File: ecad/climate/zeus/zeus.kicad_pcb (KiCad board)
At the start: 2 copper layers, 80 x 45 mm, 76 parts, among them J1 MCV 1,5/ 2-G-3,5, J10 47053-1000, J11 47053-1000, J2 MCV 1,5/ 2-G-3,5, J3 MCV 1,5/ 2-G-3,5, J4 M20-8760342, J5 47053-1000, J6 47053-1000, J7 215079-8, J8 640454-2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

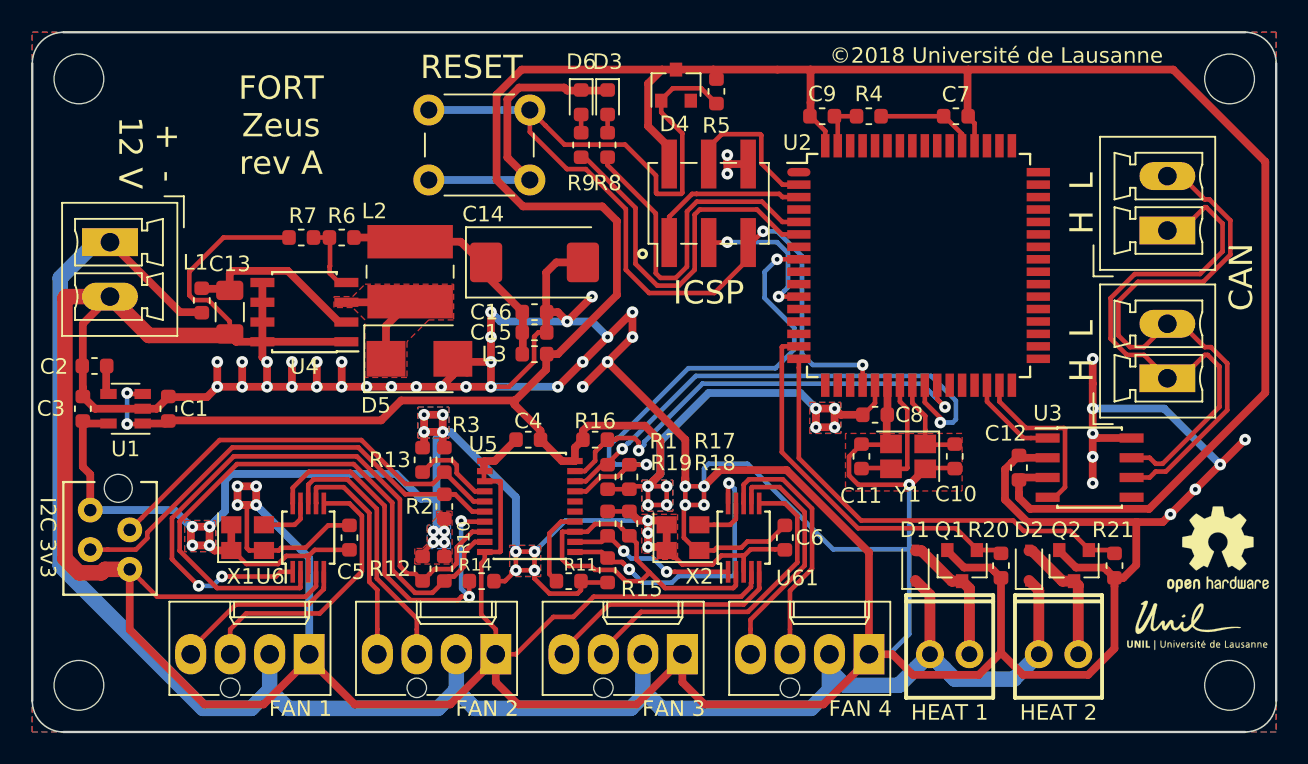
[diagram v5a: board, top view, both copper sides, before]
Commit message: Updates climate board to rev B~dev
 * Changes all Power Connectors to MiniFit-JR 5566-02A to avoid
   someone pluging the power supply on the CAN bus as it will destroy
   all MCP2561 on the bus
 * Fixes issues in Arke:
 ** Crossed Rx/Tx lines
 ** Flipped DB9 connector
 * Fixes and Improvment in Celaeno/Zeus:
 ** Added missing pull-up resistor on tachometer inputs
 ** Removed unecessary 32.268kHz oscillators (they are not working
    properly with manual soldering)
 ** Removed I2C multiplexer as we can add a second EMC2302 with a
   different i2c address to do the same thing. Repaced it by an i2c
   level shifter (tested and working).

Many of these changes still need to be tested before going to
production
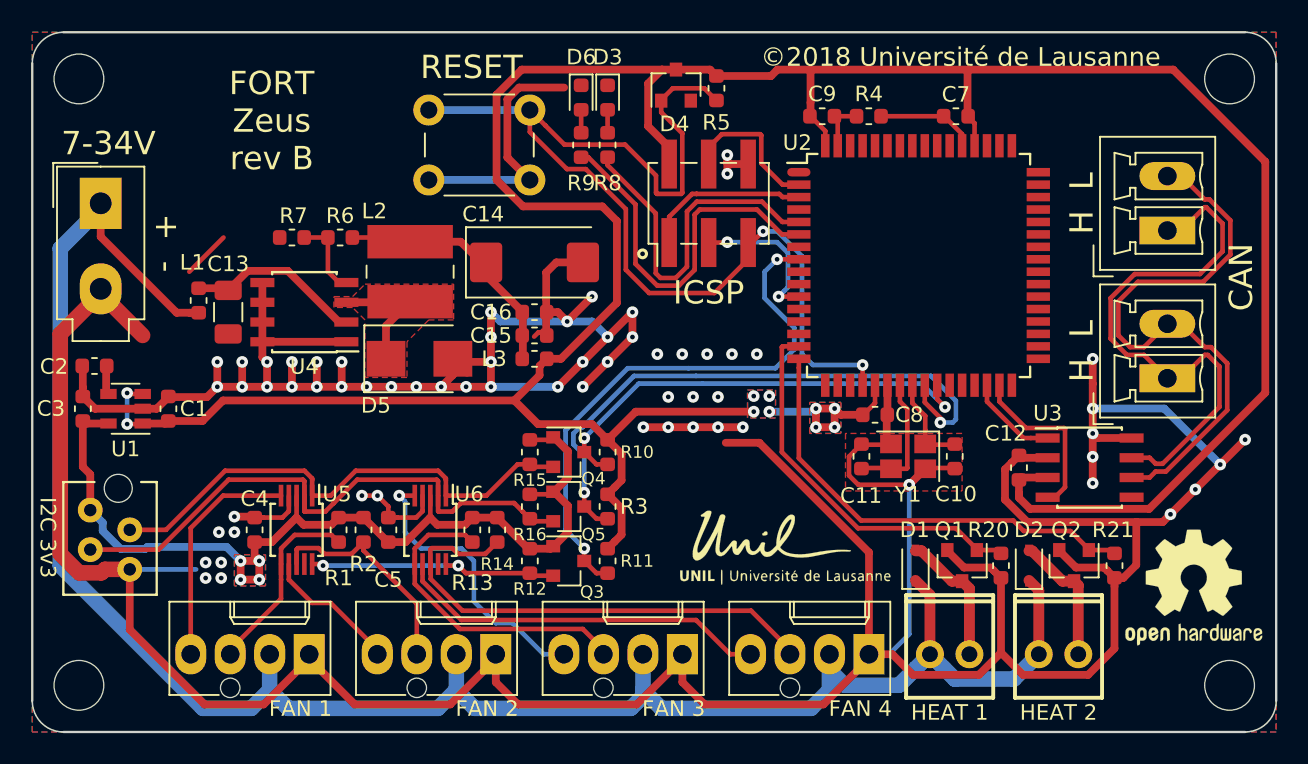
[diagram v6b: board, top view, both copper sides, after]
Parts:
- removed C6: 100nF, Capacitor_SMD:C_0603_1608Metric
- removed the G*** at (175.0, 143.2)
- removed R17, R18, R19: 10k, Resistor_SMD:R_0603_1608Metric
- removed REF***: OSHW-Logo2_7.3x6mm_SilkScreen, Symbols:OSHW-Logo2_7.3x6mm_SilkScreen
- removed U61: EMC2302-1-AIZL-TR, Package_SO:MSOP-10_3x3mm_P0.5mm
- removed X1, X2: 32.768kHz, Oscillator:Oscillator_SMD_Abracon_ASE-4Pin_3.2x2.5mm
- added G***: LOGO, FORT:UNIL-LOGO_13.8x5.1mm, F.Cu at (148.6, 138.3)
- added Q3: BSS138, Package_TO_SOT_SMD:SOT-23, F.Cu at (134.5, 139.0)
- added Q4: BSS138, Package_TO_SOT_SMD:SOT-23, F.Cu at (134.5, 132.0)
- added Q5: BSS138, Package_TO_SOT_SMD:SOT-23, F.Cu at (134.5, 135.5)
- added REF**: OSHW-Logo2_9.8x8mm_SilkScreen, Symbol:OSHW-Logo2_9.8x8mm_SilkScreen, F.Cu at (174.7, 140.7)
- J3: value MCV 1,5/ 2-G-3,5 -> 5566-02A; footprint Connector_Phoenix_MC:PhoenixContact_MCV_1,5_2-G-3.5_1x02_P3.50mm_Vertical -> FORT:Molex_Mini-Fit_Jr_5566-02A_2x01_P4.20mm_Vertical
- R12, R15, R16: value 10k -> 4k99
- R2, R3: value 4k99 -> 10k
- U5: value TCA9544A -> EMC2302-1-AIZL-TR; footprint Package_SO:SSOP-20_4.4x6.5mm_P0.65mm -> Package_SO:MSOP-10_3x3mm_P0.5mm
- U6: value EMC2302-1-AIZL-TR -> EMC2302-2-AIZL-TR
- moved C4 18.5 mm to (114.3, 137.0), turned to 90 degrees
- moved R1 17.6 mm to (119.7, 137.0)
- moved U5 15.1 mm to (117.0, 137.0), turned to 270 degrees
- moved R10 12.9 mm to (137.0, 132.0), turned to 270 degrees
- moved R3 10.9 mm to (137.0, 135.5), turned to 270 degrees
- moved R15 9.10 mm to (132.0, 132.0)
- moved U6 7.87 mm to (125.6, 137.0), turned to 270 degrees
- moved R12 6.92 mm to (132.0, 139.0), turned to 270 degrees
- moved R16 6.01 mm to (132.0, 135.5), turned to 270 degrees
- moved R13 5.52 mm to (128.3, 137.0), turned to 270 degrees
- moved R2 5.41 mm to (121.3, 137.0)
- moved R14 3.45 mm to (129.9, 137.0), turned to 270 degrees
- moved R11 2.82 mm to (137.0, 139.0), turned to 270 degrees
- moved J3 2.57 mm to (104.4, 116.0), turned to 0 degrees
- moved C5 2.55 mm to (122.9, 137.0)
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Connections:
- C4 pad 1: +5V -> +3V3
- J10 pad 3: /Fan PWM Controller 2/TACH1 -> /Fan PWM Controller 1/TACH3
- J10 pad 4: /Fan PWM Controller 2/PWM1 -> /Fan PWM Controller 1/PWM3
- J11 pad 3: /Fan PWM Controller 2/TACH2 -> /Fan PWM Controller 1/TACH4
- J11 pad 4: /Fan PWM Controller 2/PWM2 -> /Fan PWM Controller 1/PWM4
- J7 pad 2: /I2C Multiplexer/SDA_3V3_0 -> /Fan PWM Controller 1/SDA
- J7 pad 3: /I2C Multiplexer/SCL_3V3_0 -> /Fan PWM Controller 1/SCL
- R1 pad 1: /I2C Multiplexer/SCL_5V -> +3V3
- R1 pad 2: +5V -> /Fan PWM Controller 1/TACH1
- R10 pad 1: /Fan PWM Controller 1/SCL -> +5V
- R10 pad 2: +3V3 -> /I2C Level Shifter/SDA_5V
- R11 pad 1: +3V3 -> +5V
- R11 pad 2: /I2C Multiplexer/~INT3 -> /UC/~FAN_ALERT
- R12 pad 1: /Fan PWM Controller 1/SDA -> +3V3
- R12 pad 2: +3V3 -> /Fan PWM Controller 1/~ALERT
- R13 pad 1: /I2C Multiplexer/~INT0 -> +3V3
- R13 pad 2: +3V3 -> /Fan PWM Controller 1/TACH3
- R14 pad 1: /Fan PWM Controller 1/~ALERT -> +3V3
- R14 pad 2: +3V3 -> /Fan PWM Controller 1/TACH4
- R15 pad 1: /Fan PWM Controller 2/~ALERT -> +3V3
- R15 pad 2: +3V3 -> /Fan PWM Controller 1/SDA
- R16 pad 1: /I2C Multiplexer/SDA_5V -> +3V3
- R16 pad 2: +5V -> /Fan PWM Controller 1/SCL
- R2 pad 1: /I2C Multiplexer/SCL_3V3_0 -> +3V3
- R2 pad 2: +3V3 -> /Fan PWM Controller 1/TACH2
- R3 pad 1: /I2C Multiplexer/SDA_3V3_0 -> +5V
- R3 pad 2: +3V3 -> /I2C Level Shifter/SCL_5V
- U2 pad 25: /I2C Multiplexer/SCL_5V -> /I2C Level Shifter/SCL_5V
- U2 pad 26: /I2C Multiplexer/SDA_5V -> /I2C Level Shifter/SDA_5V
- U5 pad 1: GND -> /Fan PWM Controller 1/SDA
- U5 pad 10: GND -> /Fan PWM Controller 1/~ALERT
- U5 pad 2: GND -> /Fan PWM Controller 1/SCL
- U5 pad 3: GND -> +3V3
- U5 pad 4: /I2C Multiplexer/~INT0 -> GND
- U5 pad 5: /I2C Multiplexer/SDA_3V3_0 -> /Fan PWM Controller 1/PWM1
- U5 pad 6: /I2C Multiplexer/SCL_3V3_0 -> /Fan PWM Controller 1/TACH1
- U5 pad 7: /Fan PWM Controller 1/~ALERT -> /Fan PWM Controller 1/PWM2
- U5 pad 8: /Fan PWM Controller 1/SDA -> /Fan PWM Controller 1/TACH2
- U5 pad 9: /Fan PWM Controller 1/SCL -> (no net)
- U6 pad 5: /Fan PWM Controller 1/PWM1 -> /Fan PWM Controller 1/PWM3
- U6 pad 6: /Fan PWM Controller 1/TACH1 -> /Fan PWM Controller 1/TACH3
- U6 pad 7: /Fan PWM Controller 1/PWM2 -> /Fan PWM Controller 1/PWM4
- U6 pad 8: /Fan PWM Controller 1/TACH2 -> /Fan PWM Controller 1/TACH4
- U6 pad 9: /Fan PWM Controller 1/32K768_CLK -> (no net)
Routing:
- net GND: track 501.3 -> 370.7 mm, vias 50 -> 64
- net +3V3: track 119.3 -> 62.7 mm, vias 19 -> 4
- net /I2C Level Shifter/SCL_5V: track 0.00 -> 38.7 mm, vias 0 -> 2
- net /I2C Multiplexer/SCL_5V: track 33.1 -> 0.00 mm, vias 2 -> 0
- net /Fan PWM Controller 1/TACH4: track 0.00 -> 32.0 mm
- net /I2C Multiplexer/SCL_3V3_0: track 30.0 -> 0.00 mm
- net /I2C Multiplexer/SDA_5V: track 29.8 -> 0.00 mm, vias 2 -> 0
- net /I2C Level Shifter/SDA_5V: track 0.00 -> 29.6 mm, vias 0 -> 2
- net /I2C Multiplexer/SDA_3V3_0: track 27.7 -> 0.00 mm
- net /Fan PWM Controller 1/PWM4: track 0.00 -> 24.1 mm
- net /Fan PWM Controller 2/SCL: track 22.8 -> 0.00 mm
- net /Fan PWM Controller 2/TACH1: track 20.9 -> 0.00 mm
- net /Fan PWM Controller 1/TACH3: track 0.00 -> 20.7 mm
- net /Fan PWM Controller 1/PWM3: track 0.00 -> 18.9 mm, vias 0 -> 1
- net /Fan PWM Controller 2/~ALERT: track 18.7 -> 0.00 mm, vias 2 -> 0
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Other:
- board text added: "+ -"
- board text added: "7-34V"
- board text added: "FORT Zeus rev B"
- board text removed: "+ - 12 V"
- board text removed: "FORT Zeus rev A"

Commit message: Adds TVS diode on zeus output fan
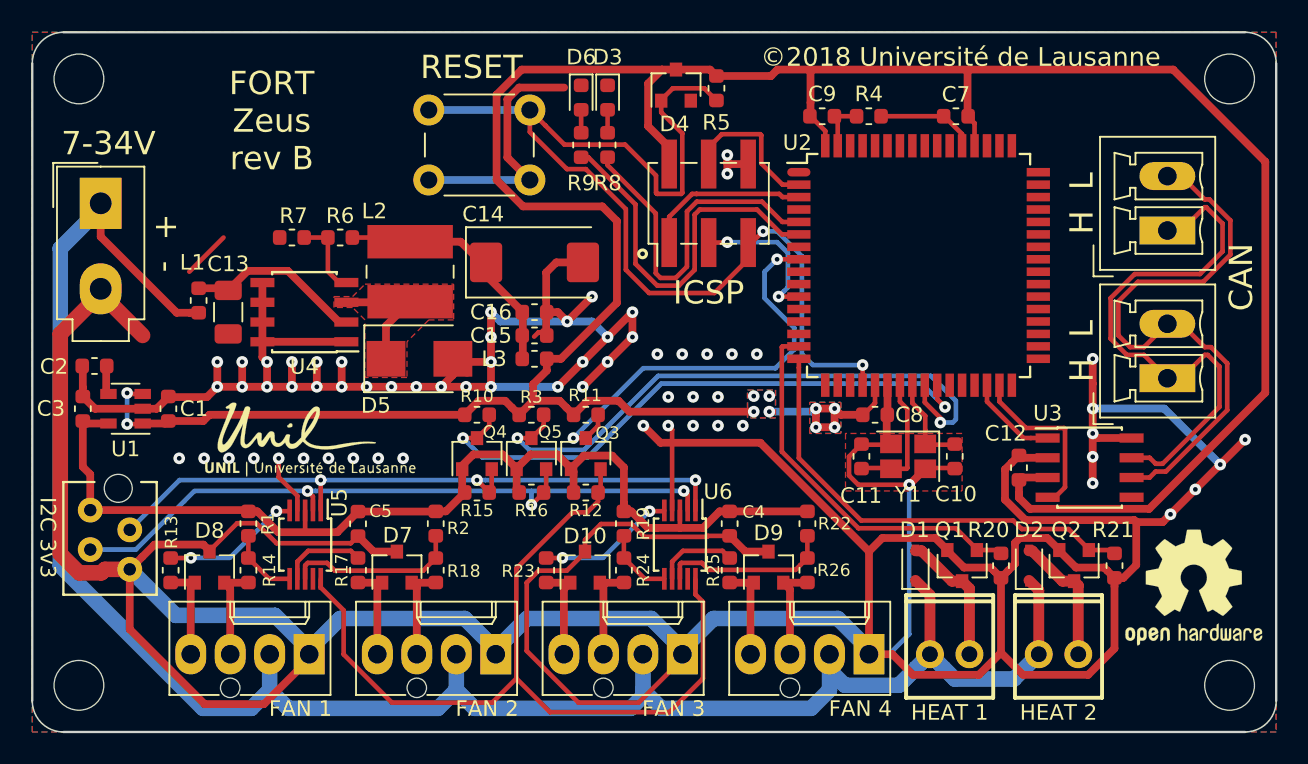
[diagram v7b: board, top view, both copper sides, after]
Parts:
- added D10: CPDT-5V0-HF, Package_TO_SOT_SMD:SOT-23, F.Cu at (135.6, 139.4)
- added D7: CPDT-5V0-HF, Package_TO_SOT_SMD:SOT-23, F.Cu at (123.5, 139.4)
- added D8: CPDT-5V0-HF, Package_TO_SOT_SMD:SOT-23, F.Cu at (111.4, 139.4)
- added D9: CPDT-5V0-HF, Package_TO_SOT_SMD:SOT-23, F.Cu at (147.3, 139.4)
- added R17: 2k2, Resistor_SMD:R_0603_1608Metric, F.Cu at (121.0, 139.6)
- added R18: 2k2, Resistor_SMD:R_0603_1608Metric, F.Cu at (126.0, 139.6)
- added R19: 47k, Resistor_SMD:R_0603_1608Metric, F.Cu at (138.1, 136.6)
- added R22: 47k, Resistor_SMD:R_0603_1608Metric, F.Cu at (149.8, 136.6)
- added R23: 2k2, Resistor_SMD:R_0603_1608Metric, F.Cu at (133.1, 139.6)
- added R24: 2k2, Resistor_SMD:R_0603_1608Metric, F.Cu at (138.1, 139.6)
- added R25: 2k2, Resistor_SMD:R_0603_1608Metric, F.Cu at (144.8, 139.6)
- added R26: 2k2, Resistor_SMD:R_0603_1608Metric, F.Cu at (149.8, 139.6)
- C15: value 4u7, 6.3V -> 100n
- C16: value 100n -> 4u7, 6.3V
- R1, R2: value 10k -> 47k
- R13, R14: value 10k -> 2k2
- moved G*** 31.3 mm to (118.0, 131.3)
- moved C4 30.6 mm to (144.8, 136.6), turned to 270 degrees
- moved R13 19.6 mm to (108.9, 139.6), turned to 90 degrees
- moved R14 16.2 mm to (113.9, 139.6), turned to 90 degrees
- moved U6 16.1 mm to (141.7, 137.9)
- moved R11 9.50 mm to (135.6, 129.6), turned to 0 degrees
- moved R10 8.74 mm to (128.6, 129.6), turned to 0 degrees
- moved R3 7.67 mm to (132.1, 129.6), turned to 0 degrees
- moved Q3 6.99 mm to (135.6, 132.1), turned to 90 degrees
- moved Q4 5.90 mm to (128.6, 132.1), turned to 90 degrees
- moved R1 5.81 mm to (113.9, 136.6)
- moved R12 5.69 mm to (135.6, 134.6), turned to 0 degrees
- moved R2 4.67 mm to (126.0, 136.6)
- moved R15 4.28 mm to (128.6, 134.6), turned to 0 degrees
- moved Q5 4.16 mm to (132.1, 132.1), turned to 90 degrees
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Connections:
- R1 pad 2: /Fan PWM Controller 1/TACH1 -> /Fan PWM Controller 1/TACH1_PR
- R13 pad 1: +3V3 -> /Fan PWM Controller 1/PWM1
- R13 pad 2: /Fan PWM Controller 1/TACH3 -> /Fan PWM Controller 1/PW1_PR
- R14 pad 1: +3V3 -> /Fan PWM Controller 1/TACH1
- R14 pad 2: /Fan PWM Controller 1/TACH4 -> /Fan PWM Controller 1/TACH1_PR
- R2 pad 2: /Fan PWM Controller 1/TACH2 -> /Fan PWM Controller 1/TACH2_PR
- U5 pad 5: /Fan PWM Controller 1/PWM1 -> /Fan PWM Controller 1/PW1_PR
- U5 pad 6: /Fan PWM Controller 1/TACH1 -> /Fan PWM Controller 1/TACH1_PR
- U5 pad 7: /Fan PWM Controller 1/PWM2 -> /Fan PWM Controller 1/PW2_PR
- U5 pad 8: /Fan PWM Controller 1/TACH2 -> /Fan PWM Controller 1/TACH2_PR
- U6 pad 5: /Fan PWM Controller 1/PWM3 -> /Fan PWM Controller 1/PW3_PR
- U6 pad 6: /Fan PWM Controller 1/TACH3 -> /Fan PWM Controller 1/TACH3_PR
- U6 pad 7: /Fan PWM Controller 1/PWM4 -> /Fan PWM Controller 1/PW4_PR
- U6 pad 8: /Fan PWM Controller 1/TACH4 -> /Fan PWM Controller 1/TACH4_PR
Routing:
- net GND: track 370.7 -> 440.9 mm, vias 64 -> 65
- net /Fan PWM Controller 1/~ALERT: track 16.7 -> 55.2 mm, vias 2 -> 0
- net /Fan PWM Controller 1/TACH4: track 32.0 -> 6.33 mm
- net /Fan PWM Controller 1/PWM4: track 24.1 -> 6.24 mm
- net /Fan PWM Controller 1/TACH3: track 20.7 -> 6.25 mm
- net /Fan PWM Controller 1/PWM3: track 18.9 -> 6.68 mm, vias 1 -> 0
- net /Fan PWM Controller 1/SDA: track 33.0 -> 44.3 mm, vias 0 -> 3
- net /Fan PWM Controller 1/TACH2_PR: track 0.00 -> 11.3 mm
- net /Fan PWM Controller 1/TACH4_PR: track 0.00 -> 11.1 mm
- net +5V: track 203.0 -> 194.0 mm
- net /Fan PWM Controller 1/PW1_PR: track 0.00 -> 8.92 mm, vias 0 -> 2
- net /Fan PWM Controller 1/PW3_PR: track 0.00 -> 8.87 mm, vias 0 -> 2
- net /I2C Level Shifter/SDA_5V: track 29.6 -> 38.4 mm
- net /Fan PWM Controller 1/PWM1: track 14.8 -> 6.26 mm
- net /UC/~FAN_ALERT: track 35.9 -> 27.5 mm
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- removed copper zone on B.Cu, net +3V3
- removed copper zone on F.Cu, net +3V3

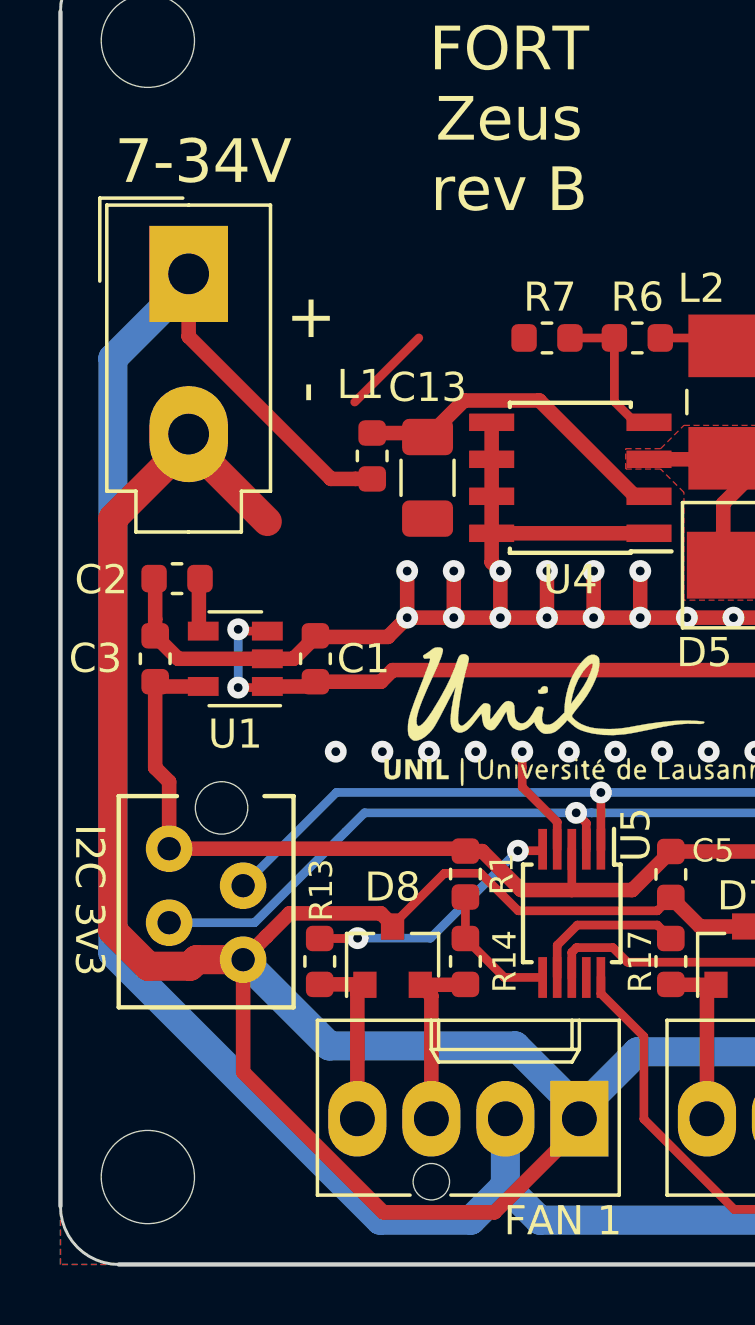
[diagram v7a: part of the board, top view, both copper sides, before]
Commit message: Adds TVS on Zeus I2C bus
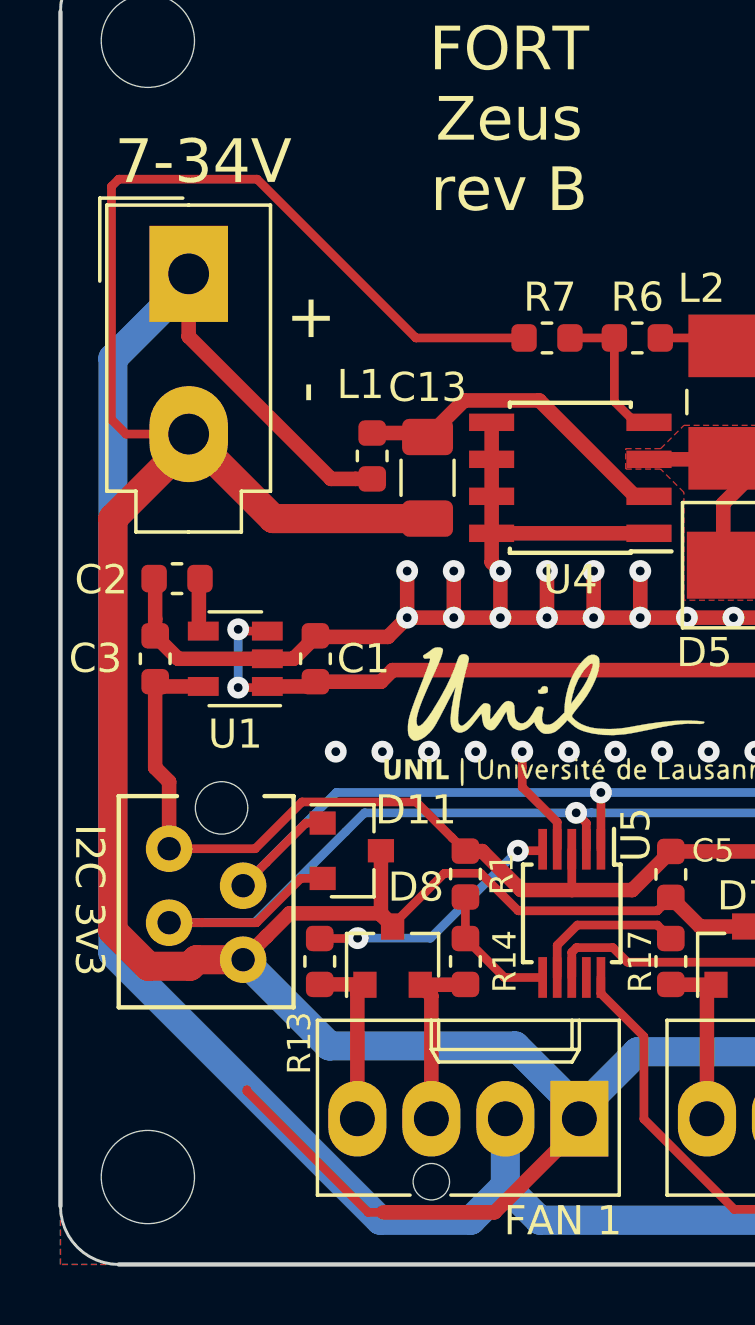
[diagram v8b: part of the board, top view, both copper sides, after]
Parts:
- added D11: CPDT-5V0USP-HF, Package_TO_SOT_SMD:SOT-23, F.Cu at (110.0, 135.8)
- C15: value 100n -> 4u7, 6.3V
- C16: value 4u7, 6.3V -> 100n
- D10, D7, D8, D9: value CPDT-5V0-HF -> CPDT-5V0USP-HF
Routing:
- net GND: track 440.9 -> 469.3 mm
- net /Fan PWM Controller 1/SCL: track 46.1 -> 52.0 mm
- net /Fan PWM Controller 1/SDA: track 44.3 -> 47.9 mm
- net +3V3: track 69.0 -> 70.3 mm
